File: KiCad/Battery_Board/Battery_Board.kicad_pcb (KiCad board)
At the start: 4 copper layers, 101.6 x 63.5 mm, 13 parts, among them P1 CONN_LEFT_TOP, P2 CONN_RIGHT_TOP, P3 CONN_LEFT_BOTTOM, P4 CONN_RIGHT_BOTTOM

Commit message: Created & assigned footprints.
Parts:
- added C1: 1uF, Capacitors_SMD:C_0603, F.Cu at (125.5, 146.6)
- added C2: 4.7uF, Capacitors_SMD:C_0805, F.Cu at (178.1, 148.3)
- added C3: 1uF, Capacitors_SMD:C_0603, F.Cu at (176.4, 155.2)
- added C4: 10nF, Capacitors_SMD:C_0603, F.Cu at (111.4, 156.7)
- added C5: 4.7uF, Capacitors_SMD:C_0805, F.Cu at (134.1, 173.0)
- added D1: RG_LED, OpenCamera:RG_LED, F.Cu at (156.3, 117.5)
- added P5: CONN_01X02, OpenCamera:JST-2, F.Cu at (138.0, 117.5)
- added R1: 10k, Resistors_SMD:R_0402, F.Cu at (134.4, 157.5)
- added R10: 1.5k, Resistors_SMD:R_0402, F.Cu at (155.6, 144.5)
- added R11: DNP, Resistors_SMD:R_0805, F.Cu at (148.1, 159.8)
- added R12: DNP, Resistors_SMD:R_0805, F.Cu at (136.9, 144.8)
- added R13: DNP, Resistors_SMD:R_0805, F.Cu at (120.9, 152.8)
- added R14: DNP, Resistors_SMD:R_0805, F.Cu at (198.5, 161.0)
- added R15: 0, Resistors_SMD:R_0805, F.Cu at (160.4, 155.3)
- added R2: 1k, Resistors_SMD:R_0402, F.Cu at (106.8, 145.5)
- added R3: 1.74k, Resistors_SMD:R_0402, F.Cu at (122.8, 165.2)
- added R4: DNP, Resistors_SMD:R_0805, F.Cu at (159.6, 163.8)
- added R5: DNP, Resistors_SMD:R_0805, F.Cu at (164.7, 146.9)
- added R6: 150, Resistors_SMD:R_0402, F.Cu at (145.9, 178.7)
- added R7: 0, Resistors_SMD:R_0805, F.Cu at (135.9, 151.3)
- added R8: DNP, Resistors_SMD:R_0805, F.Cu at (176.0, 165.9)
- added R9: 1.5k, Resistors_SMD:R_0402, F.Cu at (148.1, 151.5)
- added U1: BQ24230, OpenCamera:BQ24230, F.Cu at (154.4, 171.6)
- added U2: MAX17043, OpenCamera:MAX17043, F.Cu at (154.6, 150.5)
- added USB1: USB_Micro_B_Receptacle, OpenCamera:MicroUSB-B-Receptacle, F.Cu at (152.1, 131.4)
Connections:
- P1 pad 1: GNDD -> GND
- P1 pad 11: GNDD -> GND
- P1 pad 13: GNDD -> GND
- P1 pad 15: GNDD -> GND
- P1 pad 17: GNDD -> GND
- P1 pad 19: GNDD -> GND
- P1 pad 21: GNDD -> GND
- P1 pad 23: GNDD -> GND
- P1 pad 25: GNDD -> GND
- P1 pad 27: GNDD -> GND
- P1 pad 29: GNDD -> GND
- P1 pad 3: GNDD -> GND
- P1 pad 31: GNDD -> GND
- P1 pad 33: GNDD -> GND
- P1 pad 35: GNDD -> GND
- P1 pad 37: GNDD -> GND
- P1 pad 39: GNDD -> GND
- P1 pad 41: GNDD -> GND
- P1 pad 43: GNDD -> GND
- P1 pad 45: GNDD -> GND
- P1 pad 47: GNDD -> GND
- P1 pad 49: GNDD -> GND
- P1 pad 5: GNDD -> GND
- P1 pad 51: GNDD -> GND
- P1 pad 53: GNDD -> GND
- P1 pad 55: GNDD -> GND
- P1 pad 57: GNDD -> GND
- P1 pad 59: GNDD -> GND
- P1 pad 61: GNDD -> GND
- P1 pad 62: GNDD -> GND
- P1 pad 7: GNDD -> GND
- P1 pad 9: GNDD -> GND
- P2 pad 10: GNDA -> GND
- P2 pad 12: GNDA -> GND
- P2 pad 14: GNDA -> GND
- P2 pad 16: GNDA -> GND
- P2 pad 18: GNDA -> GND
- P2 pad 2: GNDA -> GND
- P2 pad 20: GNDA -> GND
- P2 pad 22: GNDA -> GND
- P2 pad 24: GNDA -> GND
- P2 pad 26: GNDA -> GND
- P2 pad 28: GNDA -> GND
- P2 pad 30: GNDA -> GND
- P2 pad 32: GNDA -> GND
- P2 pad 34: GNDA -> GND
- P2 pad 36: GNDA -> GND
- P2 pad 38: GNDA -> GND
- P2 pad 4: GNDA -> GND
- P2 pad 40: GNDA -> GND
- P2 pad 42: GNDA -> GND
- P2 pad 44: GNDA -> GND
- P2 pad 46: GNDA -> GND
- P2 pad 48: GNDA -> GND
- P2 pad 50: GNDA -> GND
- P2 pad 52: GNDA -> GND
- P2 pad 54: GNDA -> GND
- P2 pad 56: GNDA -> GND
- P2 pad 58: GNDA -> GND
- P2 pad 6: GNDA -> GND
- P2 pad 60: GNDA -> GND
- P2 pad 61: GNDA -> GND
- P2 pad 62: GNDA -> GND
- P2 pad 8: GNDA -> GND
- P3 pad 10: GNDD -> GND
- P3 pad 12: GNDD -> GND
- P3 pad 14: GNDD -> GND
- P3 pad 16: GNDD -> GND
- P3 pad 18: GNDD -> GND
- P3 pad 2: GNDD -> GND
- P3 pad 20: GNDD -> GND
- P3 pad 22: GNDD -> GND
- P3 pad 24: GNDD -> GND
- P3 pad 26: GNDD -> GND
- P3 pad 28: GNDD -> GND
- P3 pad 30: GNDD -> GND
- P3 pad 32: GNDD -> GND
- P3 pad 34: GNDD -> GND
- P3 pad 36: GNDD -> GND
- P3 pad 38: GNDD -> GND
- P3 pad 4: GNDD -> GND
- P3 pad 40: GNDD -> GND
- P3 pad 42: GNDD -> GND
- P3 pad 44: GNDD -> GND
- P3 pad 46: GNDD -> GND
- P3 pad 48: GNDD -> GND
- P3 pad 50: GNDD -> GND
- P3 pad 52: GNDD -> GND
- P3 pad 54: GNDD -> GND
- P3 pad 56: GNDD -> GND
- P3 pad 58: GNDD -> GND
- P3 pad 6: GNDD -> GND
- P3 pad 60: GNDD -> GND
- P3 pad 61: GNDD -> GND
- P3 pad 62: GNDD -> GND
- P3 pad 8: GNDD -> GND
- P4 pad 1: GNDA -> GND
- P4 pad 11: GNDA -> GND
- P4 pad 13: GNDA -> GND
- P4 pad 15: GNDA -> GND
- P4 pad 17: GNDA -> GND
- P4 pad 19: GNDA -> GND
- P4 pad 21: GNDA -> GND
- P4 pad 23: GNDA -> GND
- P4 pad 25: GNDA -> GND
- P4 pad 27: GNDA -> GND
- P4 pad 29: GNDA -> GND
- P4 pad 3: GNDA -> GND
- P4 pad 31: GNDA -> GND
- P4 pad 33: GNDA -> GND
- P4 pad 35: GNDA -> GND
- P4 pad 37: GNDA -> GND
- P4 pad 39: GNDA -> GND
- P4 pad 41: GNDA -> GND
- P4 pad 43: GNDA -> GND
- P4 pad 45: GNDA -> GND
- P4 pad 47: GNDA -> GND
- P4 pad 49: GNDA -> GND
- P4 pad 5: GNDA -> GND
- P4 pad 51: GNDA -> GND
- P4 pad 53: GNDA -> GND
- P4 pad 55: GNDA -> GND
- P4 pad 57: GNDA -> GND
- P4 pad 59: GNDA -> GND
- P4 pad 61: GNDA -> GND
- P4 pad 62: GNDA -> GND
- P4 pad 7: GNDA -> GND
- P4 pad 9: GNDA -> GND

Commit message: Added power switch.
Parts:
- added SW1: SPST, OpenCamera:SWITCH_SPST, F.Cu at (109.1, 87.0)
- moved U2 57.6 mm to (117.9, 106.0)
- moved USB1 55.7 mm to (133.0, 79.1), turned to 180 degrees
- moved D1 50.1 mm to (123.3, 79.7)
- moved P5 17.7 mm to (130.7, 133.6), turned to 90 degrees
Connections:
- C5 pad 1: /connectors/L1 -> /Vsys
- D1 pad 1: /connectors/L1 -> /Vsys
- R13 pad 1: /connectors/L1 -> /Vsys
- R7 pad 1: /connectors/L1 -> /Vsys
- U1 pad 10: /connectors/L1 -> /Vsys
- U1 pad 11: /connectors/L1 -> /Vsys
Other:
- board text added: "LiPo Battery"

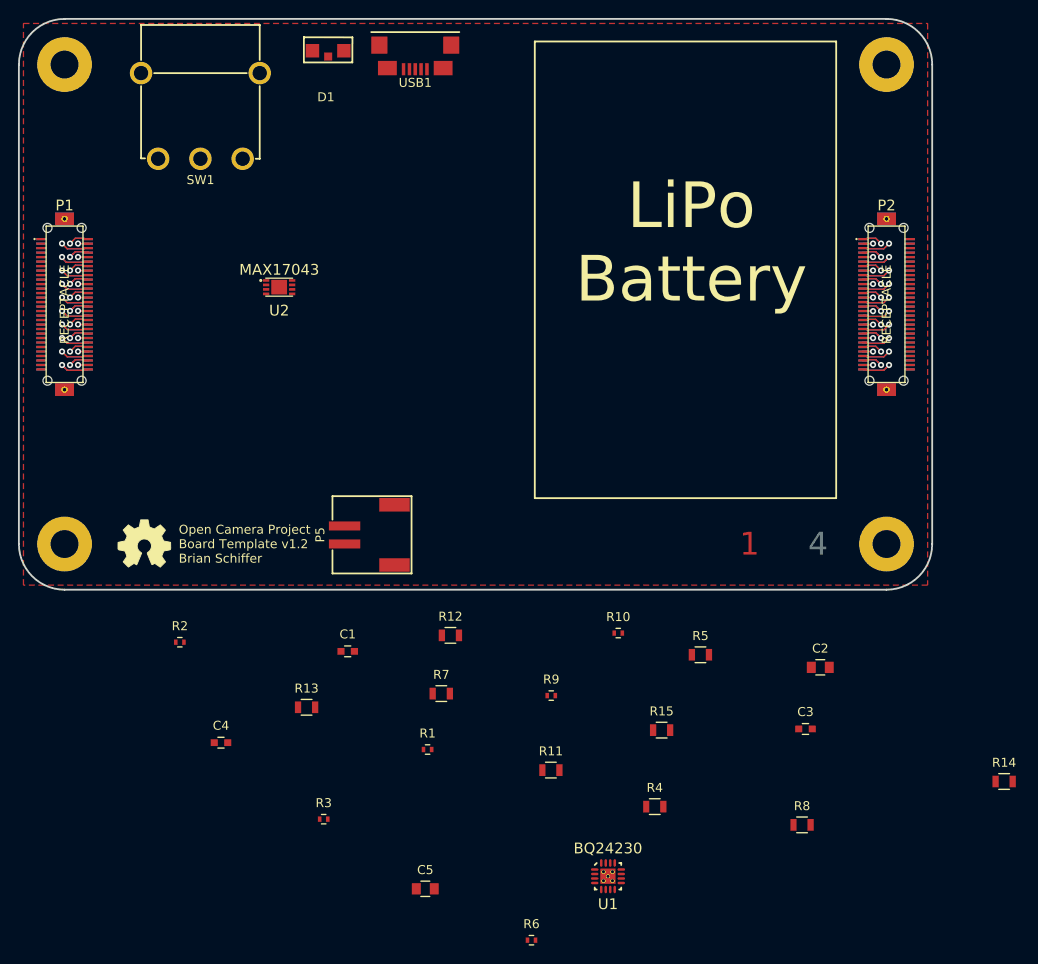
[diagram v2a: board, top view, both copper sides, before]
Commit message: Initial part placement.
Also added cutouts around the battery for a battery strap.
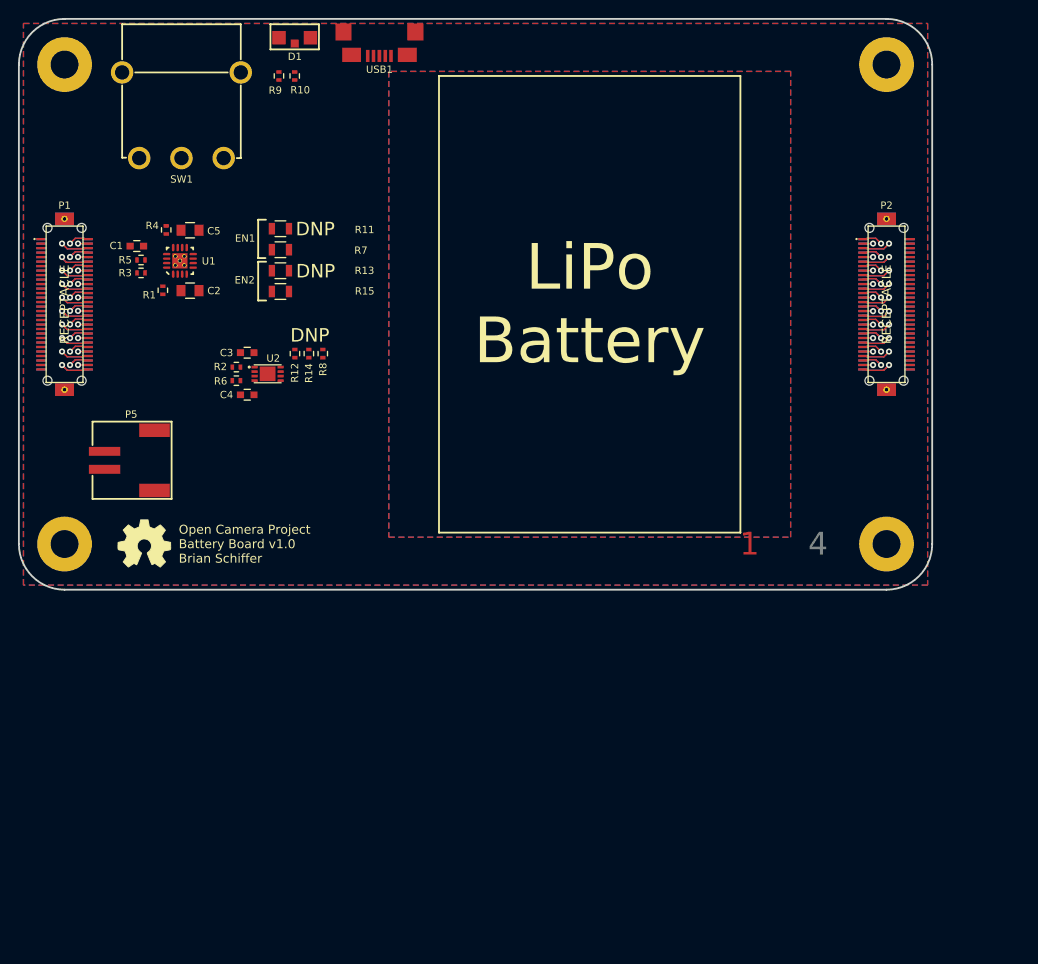
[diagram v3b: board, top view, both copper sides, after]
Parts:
- R12, R14, R4, R5, R8: footprint Resistors_SMD:R_0805 -> Resistors_SMD:R_0402
- moved R14 90.8 mm to (121.2, 113.4), turned to 270 degrees
- moved R4 84.1 mm to (105.3, 99.7), turned to 90 degrees
- moved U1 83.4 mm to (106.8, 103.1), turned to 90 degrees
- moved C2 81.7 mm to (107.9, 106.4)
- moved C5 77.8 mm to (107.9, 99.7)
- moved R5 76.2 mm to (102.5, 103.0), turned to 180 degrees
- moved R9 75.3 mm to (117.8, 82.5), turned to 90 degrees
- moved C3 74.9 mm to (114.3, 113.3)
- moved R8 74.8 mm to (122.7, 113.4), turned to 270 degrees
- moved R10 71.7 mm to (119.6, 82.5), turned to 90 degrees
- moved R6 70.4 mm to (113.1, 116.4)
- moved R11 67.3 mm to (118.0, 99.5), turned to 180 degrees
- moved R15 64.6 mm to (118.0, 106.5), turned to 180 degrees
- moved R3 64.1 mm to (102.5, 104.5), turned to 180 degrees
- moved R1 59.0 mm to (104.9, 106.4), turned to 90 degrees
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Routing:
- added copper zone on B.Cu, net GND
- added copper zone on F.Cu, net GND
- removed copper zone on F.Cu, net GNDD
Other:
- board text added: "CUT OUT"
- board text added: "DNP"
- board text added: "EN1"
- board text added: "EN2"
- board text added: "Open Camera Project Battery Board v1.0 Brian Schiffer"
- board text removed: "Open Camera Project Board Template v1.2 Brian Schiffer"

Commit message: Completed routing for battery board.
No DRC errors!
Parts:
- added ?: , OpenCamera:STITCH_VIA, F.Cu at (111.2, 100.8)
- added ?: , OpenCamera:STITCH_VIA, F.Cu at (104.9, 108.0)
- added ?: , OpenCamera:STITCH_VIA, F.Cu at (99.1, 104.3)
- added ?: , OpenCamera:STITCH_VIA, F.Cu at (99.1, 102.9)
- added ?: , OpenCamera:STITCH_VIA, F.Cu at (117.6, 118.0)
- added ?: , OpenCamera:STITCH_VIA, F.Cu at (116.6, 118.0)
- added ?: , OpenCamera:STITCH_VIA, F.Cu at (98.3, 100.3)
- added ?: , OpenCamera:STITCH_VIA, F.Cu at (99.2, 99.4)
- added ?: , OpenCamera:STITCH_VIA, F.Cu at (98.3, 99.4)
- added ?: , OpenCamera:STITCH_VIA, F.Cu at (117.8, 112.2)
- added ?: , OpenCamera:STITCH_VIA, F.Cu at (110.3, 101.8)
- added ?: , OpenCamera:STITCH_VIA, F.Cu at (116.4, 112.2)
- added ?: , OpenCamera:STITCH_VIA, F.Cu at (97.3, 99.4)
- added ?: , OpenCamera:STITCH_VIA, F.Cu at (116.6, 115.6)
- added ?: , OpenCamera:STITCH_VIA, F.Cu at (102.9, 99.9)
- added ?: , OpenCamera:STITCH_VIA, F.Cu at (110.4, 98.3)
- added ?: , OpenCamera:STITCH_VIA, F.Cu at (119.0, 97.9)
- added ?: , OpenCamera:STITCH_VIA, F.Cu at (120.4, 106.5)
- added ?: , OpenCamera:STITCH_VIA, F.Cu at (111.8, 107.8)
- added ?: , OpenCamera:STITCH_VIA, F.Cu at (110.4, 107.8)
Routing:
- net /BATT+: track 0.00 -> 53.1 mm
- net /Vsys: track 0.00 -> 47.5 mm, vias 0 -> 1
- net /Vusb: track 0.00 -> 42.6 mm, vias 0 -> 2
- net /connectors/L28: track 4.55 -> 37.3 mm, vias 1 -> 3
- net /connectors/L29: track 2.23 -> 33.0 mm, vias 1 -> 3
- net /connectors/L30: track 6.34 -> 34.3 mm, vias 1 -> 3
- net Net-(R9-Pad1): track 0.00 -> 25.7 mm, vias 0 -> 2
- net Net-(R10-Pad1): track 0.00 -> 24.3 mm
- net GND: track 0.00 -> 21.8 mm
- net Net-(R11-Pad2): track 0.00 -> 11.7 mm
- net Net-(R13-Pad2): track 0.00 -> 11.2 mm
- net Net-(D1-Pad3): track 0.00 -> 3.81 mm
- net Net-(C3-Pad1): track 0.00 -> 3.39 mm
- net Net-(C4-Pad1): track 0.00 -> 3.36 mm
- net Net-(D1-Pad2): track 0.00 -> 3.15 mm
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- added copper zone on F.Cu, net /BATT+
- added copper zone on F.Cu, net /Vsys
- added copper zone on B.Cu, net /connectors/L1
- added copper zone on F.Cu, net /connectors/L1
